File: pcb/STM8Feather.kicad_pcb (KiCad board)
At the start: 2 copper layers, 50.8 x 22.9 mm, 33 parts, among them J1 feather long, J2 feather short, J3 USB_B_Micro, J4 Conn_01x02, J5 Conn_01x04, U1 STM8S003K3T, U2 MCP73831-2-OT, U3 MIC5504-3.3YM5, U4 CH330N, Y1 Crystal

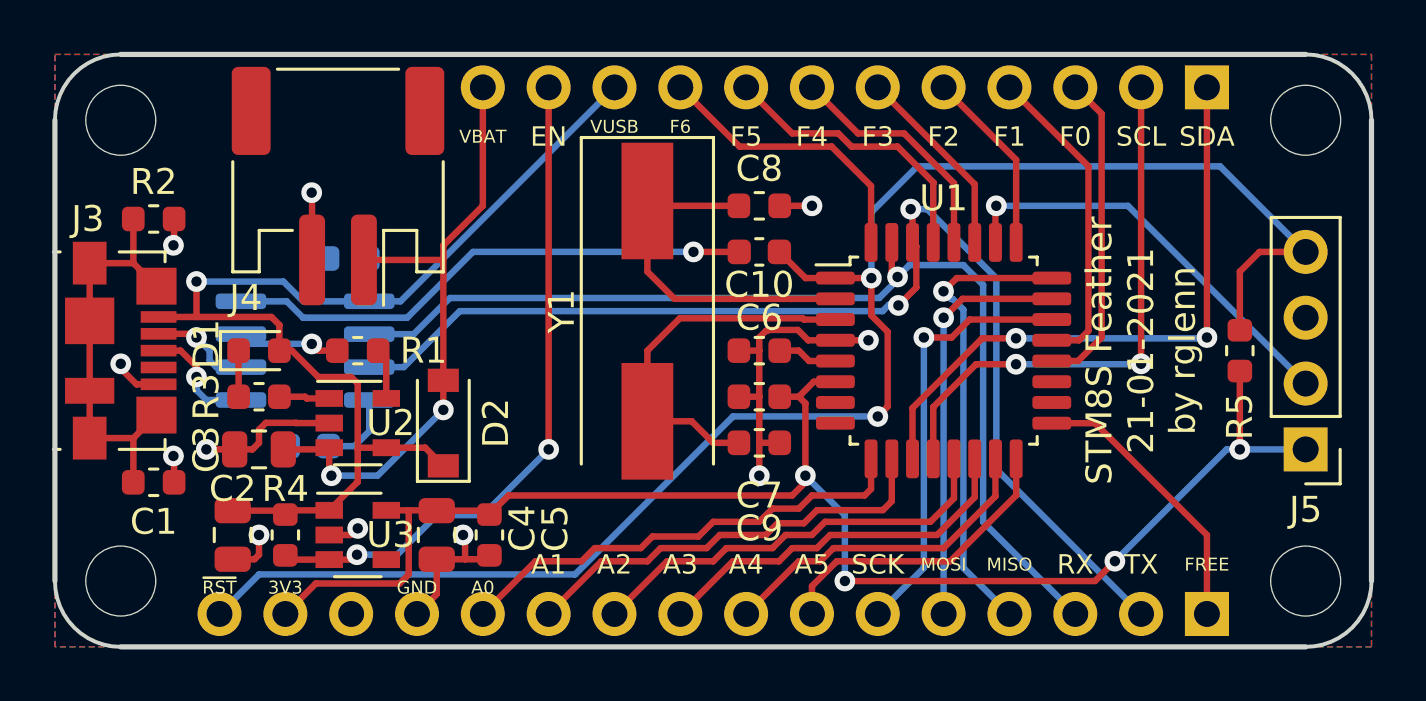
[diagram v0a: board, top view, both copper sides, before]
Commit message: Adding status LED, reset button, boot button, and power LED
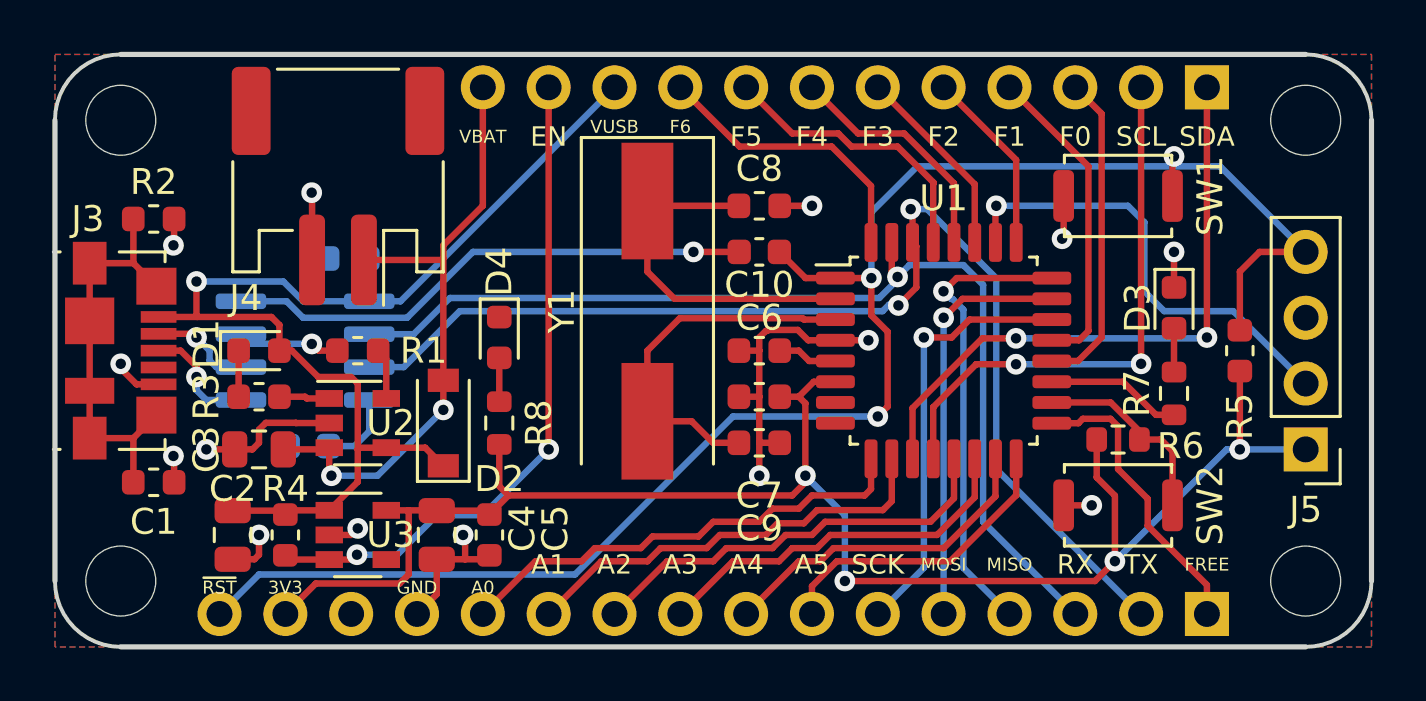
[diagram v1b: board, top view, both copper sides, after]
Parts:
- added D3: LED, LED_SMD:LED_0603_1608Metric, F.Cu at (68.6, 35.2)
- added D4: LED, LED_SMD:LED_0603_1608Metric, F.Cu at (42.5, 36.3)
- added R6: 10K, Resistor_SMD:R_0603_1608Metric, F.Cu at (66.4, 40.3)
- added R7: 1K, Resistor_SMD:R_0603_1608Metric, F.Cu at (68.6, 38.5)
- added R8: 1K, Resistor_SMD:R_0603_1608Metric, F.Cu at (42.5, 39.6)
- added SW1: SW_Push, Button_Switch_SMD:SW_Push_SPST_NO_Alps_SKRK, F.Cu at (66.4, 30.9)
- added SW2: SW_Push, Button_Switch_SMD:SW_Push_SPST_NO_Alps_SKRK, F.Cu at (66.4, 42.8)
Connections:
- U1 pad 18: (no net) -> /BOOT
- U1 pad 19: (no net) -> /STATUS
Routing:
- net /BOOT: track 0.00 -> 7.71 mm
- net +3V3: track 58.0 -> 65.1 mm
- net /STATUS: track 0.00 -> 5.24 mm
- net GND: track 38.5 -> 42.6 mm, vias 12 -> 15
- net /RESET: track 64.8 -> 66.7 mm, vias 2 -> 3
- net Net-(D4-Pad2): track 0.00 -> 1.69 mm
- net Net-(D3-Pad2): track 0.00 -> 1.69 mm
- net /SWIM: track 16.2 -> 17.8 mm
- net /FREE: track 10.8 -> 11.4 mm
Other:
- board text added: "STM8S Feather by rglenn 2021-03-25"
- board text removed: "STM8S Feather 21-01-2021 by rglenn"
